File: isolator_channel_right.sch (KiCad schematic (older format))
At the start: 44 parts, among them U301 NE5532, U302 NE5532, U303 NE5532, U304 NE5532, U305 NE5532, U306 NE5532, U307 NE5532, U308 NE5532

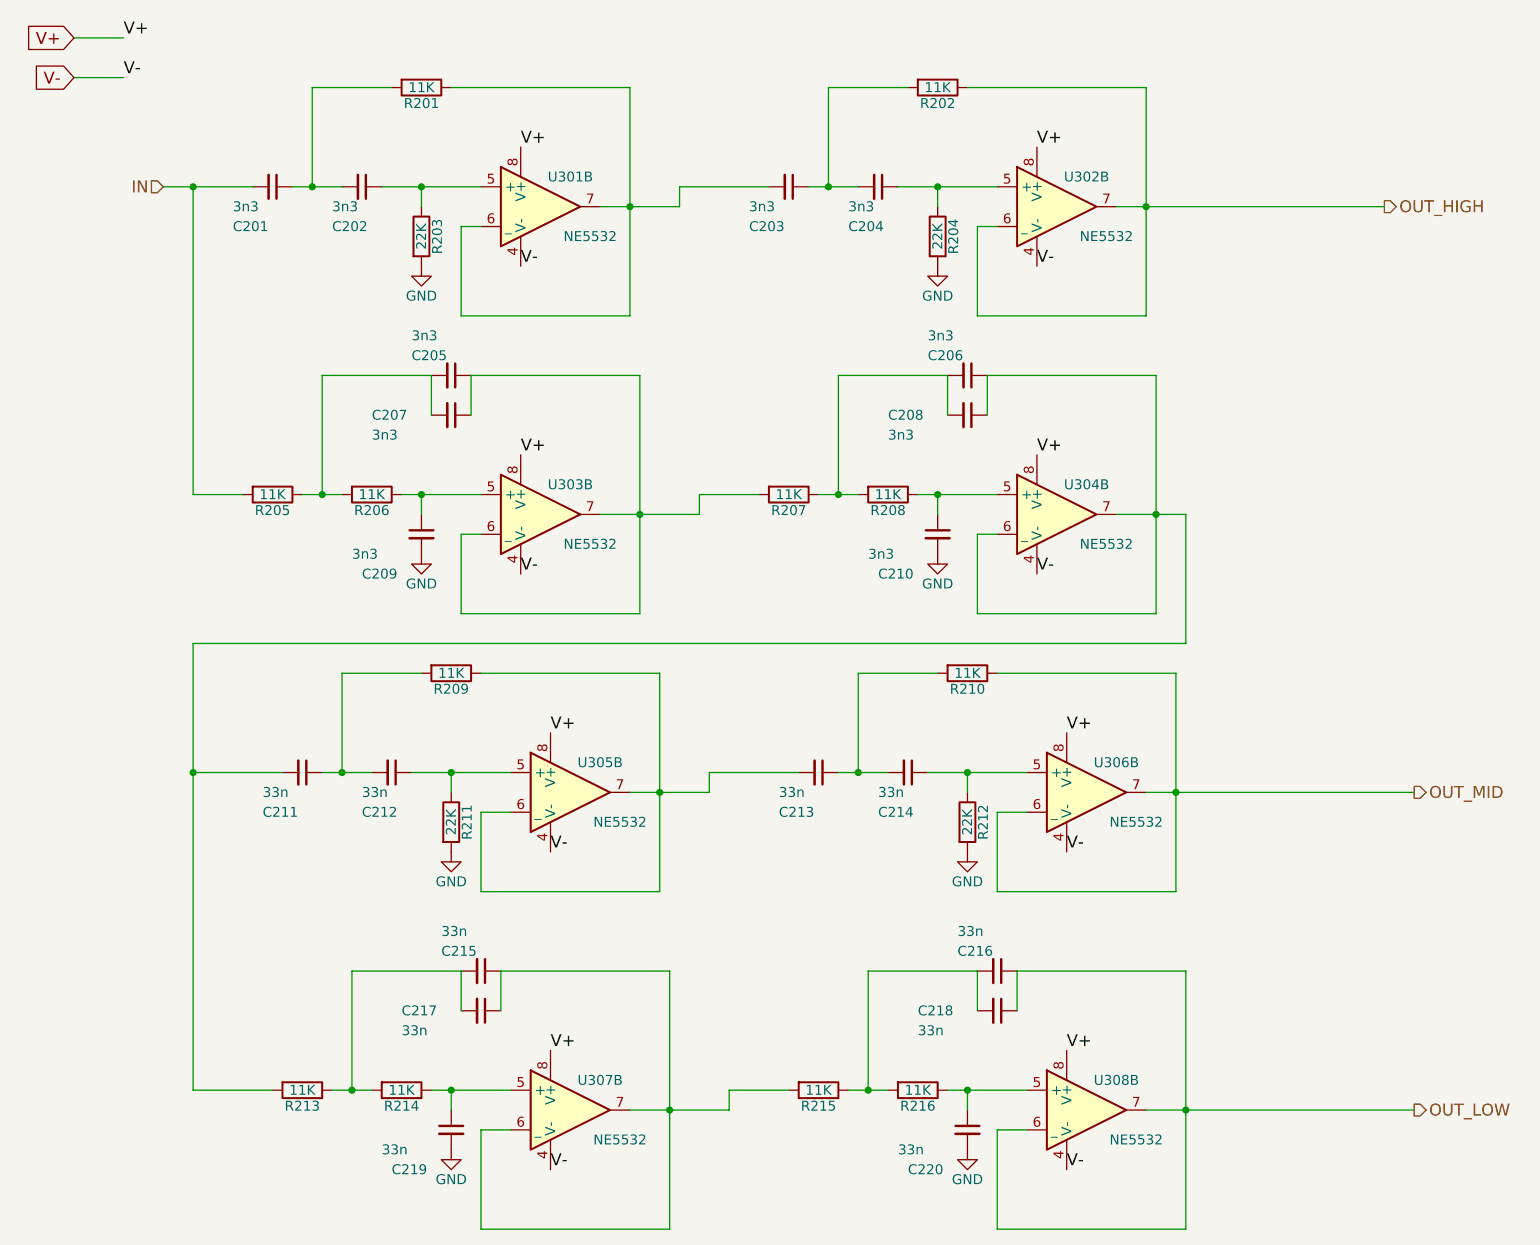
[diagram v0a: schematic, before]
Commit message: Adding active components references
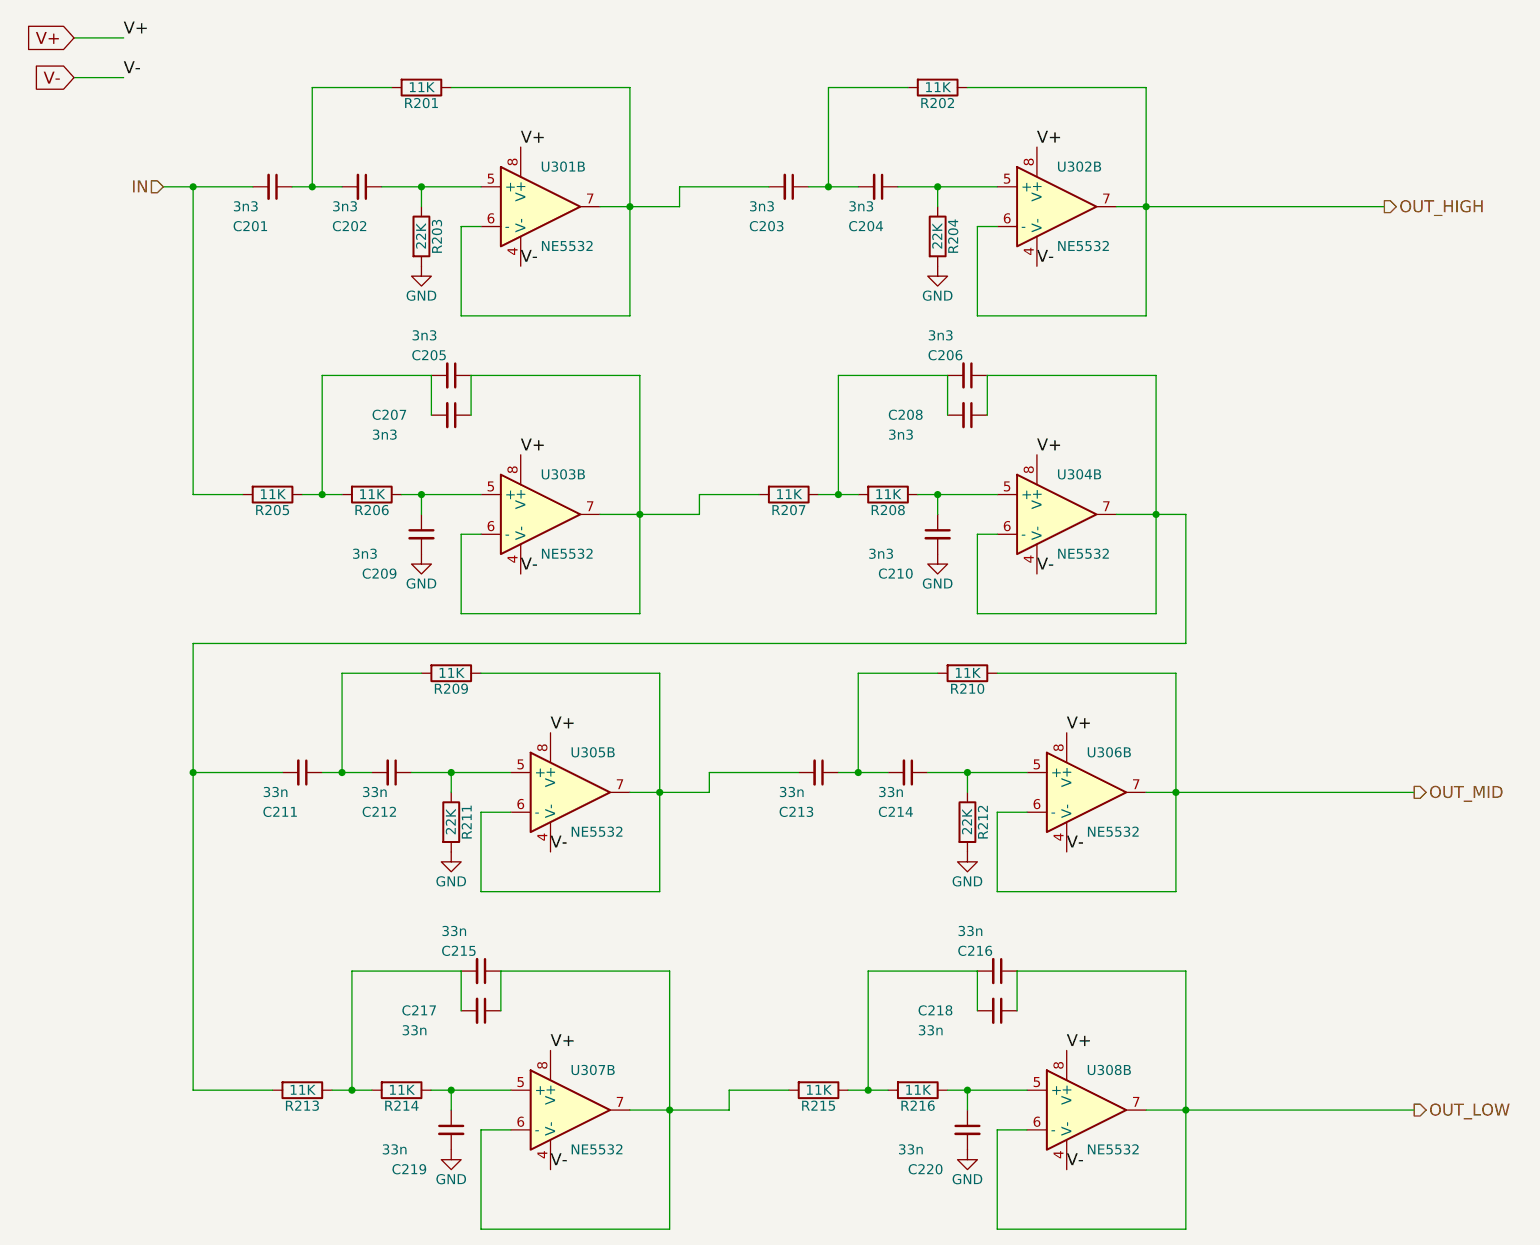
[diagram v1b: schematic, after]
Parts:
- removed U301, U302, U303, U304, U305, U306, U307, U308: NE5532, Housings_DIP:DIP-8_W7.62mm_LongPads, symbol NE5532-RESCUE-isolator
- added U301, U302, U303, U304, U305, U306, U307, U308: NE5532, Housings_DIP:DIP-8_W7.62mm_LongPads, symbol NE5532
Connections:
- net OUT_HIGH: now also U302.6 (-), U302.7
- net OUT_LOW: now also U308.6 (-), U308.7
- net OUT_MID: now also U306.6 (-), U306.7
- net V+: now also U301.8 (V+), U302.8 (V+), U303.8 (V+), U304.8 (V+), U305.8 (V+), U306.8 (V+), U307.8 (V+), U308.8 (V+)
- net V-: now also U301.4 (V-), U302.4 (V-), U303.4 (V-), U304.4 (V-), U305.4 (V-), U306.4 (V-), U307.4 (V-), U308.4 (V-)
- net at C202.1, R203.1: now also U301.5 (+)
- net at C203.2, R201.1: now also U301.6 (-), U301.7
- net at C205.1, C207.1, R207.2: now also U303.6 (-), U303.7
- net at C206.1, C208.1, C211.2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: now also U304.6 (-), U304.7
- net at C212.1, R211.1: now also U305.5 (+)
- net at C213.2, R209.1: now also U305.6 (-), U305.7
- net at C219.1, R214.1: now also U307.5 (+)
- net at C220.1, R216.1: now also U308.5 (+)
- net at C204.1, R204.1: now also U302.5 (+)
- net at C209.1, R206.1: now also U303.5 (+)
- net at C210.1, R208.1: now also U304.5 (+)
- net at C214.1, R212.1: now also U306.5 (+)
- net at C215.1, C217.1, R215.2: now also U307.6 (-), U307.7
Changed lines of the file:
@@
 Text HLabel 7650 6150 2    60   Output ~ 0
 OUT_LOW
-$Comp
-L NE5532-RESCUE-isolator U301
-U 2 1 56D773DB
-P 3250 1600
-AR Path="/56D7589A/56D773DB" Ref="U301"  Part="2"
-AR Path="/56D7630B/56D773DB" Ref="U301"  Part="1"
-AR Path="/56D773DB" Ref="U301"  Part="2"
-F 0 "U301" H 3400 1750 50  0000 C CNN
-F 1 "NE5532" H 3500 1450 50  0000 C CNN
-F 2 "Housings_DIP:DIP-8_W7.62mm_LongPads" H 3250 1600 50  0001 C CNN
-F 3 "" H 3250 1600 50  0000 C CNN
-F 4 "NE5532P" H 3250 1600 60  0001 C CNN "Mfg_Part_No"
-	2    3250 1600
-	1    0    0    -1
-$EndComp
-$Comp
-L NE5532-RESCUE-isolator U302
-U 2 1 56D775D7
-P 5850 1600
-AR Path="/56D7589A/56D775D7" Ref="U302"  Part="2"
-AR Path="/56D7630B/56D775D7" Ref="U302"  Part="1"
-AR Path="/56D775D7" Ref="U302"  Part="2"
-F 0 "U302" H 6000 1750 50  0000 C CNN
-F 1 "NE5532" H 6100 1450 50  0000 C CNN
-F 2 "Housings_DIP:DIP-8_W7.62mm_LongPads" H 5850 1600 50  0001 C CNN
-F 3 "" H 5850 1600 50  0000 C CNN
-F 4 "NE5532P" H 5850 1600 60  0001 C CNN "Mfg_Part_No"
-	2    5850 1600
-	1    0    0    -1
-$EndComp
-$Comp
-L NE5532-RESCUE-isolator U303
-U 2 1 56D776FA
-P 3250 3150
-AR Path="/56D7589A/56D776FA" Ref="U303"  Part="2"
-AR Path="/56D7630B/56D776FA" Ref="U303"  Part="1"
-AR Path="/56D776FA" Ref="U303"  Part="2"
-F 0 "U303" H 3400 3300 50  0000 C CNN
-F 1 "NE5532" H 3500 3000 50  0000 C CNN
-F 2 "Housings_DIP:DIP-8_W7.62mm_LongPads" H 3250 3150 50  0001 C CNN
-F 3 "" H 3250 3150 50  0000 C CNN
-F 4 "NE5532P" H 3250 3150 60  0001 C CNN "Mfg_Part_No"
-	2    3250 3150
-	1    0    0    -1
-$EndComp
-$Comp
-L NE5532-RESCUE-isolator U304
-U 2 1 5707D571
-P 5850 3150
-AR Path="/56D7589A/5707D571" Ref="U304"  Part="2"
-AR Path="/56D7630B/5707D571" Ref="U304"  Part="1"
-AR Path="/5707D571" Ref="U304"  Part="2"
-F 0 "U304" H 6000 3300 50  0000 C CNN
-F 1 "NE5532" H 6100 3000 50  0000 C CNN
-F 2 "Housings_DIP:DIP-8_W7.62mm_LongPads" H 5850 3150 50  0001 C CNN
-F 3 "" H 5850 3150 50  0000 C CNN
-F 4 "NE5532P" H 5850 3150 60  0001 C CNN "Mfg_Part_No"
-	2    5850 3150
-	1    0    0    -1
-$EndComp
-$Comp
-L NE5532-RESCUE-isolator U306
-U 2 1 5707D572
-P 6000 4550
-AR Path="/56D7589A/5707D572" Ref="U306"  Part="2"
-AR Path="/56D7630B/5707D572" Ref="U306"  Part="1"
-AR Path="/5707D572" Ref="U306"  Part="2"
-F 0 "U306" H 6150 4700 50  0000 C CNN
-F 1 "NE5532" H 6250 4400 50  0000 C CNN
-F 2 "Housings_DIP:DIP-8_W7.62mm_LongPads" H 6000 4550 50  0001 C CNN
-F 3 "" H 6000 4550 50  0000 C CNN
-F 4 "NE5532P" H 6000 4550 60  0001 C CNN "Mfg_Part_No"
-	2    6000 4550
-	1    0    0    -1
-$EndComp
-$Comp
-L NE5532-RESCUE-isolator U305
-U 2 1 5707D573
-P 3400 4550
-AR Path="/56D7589A/5707D573" Ref="U305"  Part="2"
-AR Path="/56D7630B/5707D573" Ref="U305"  Part="1"
-AR Path="/5707D573" Ref="U305"  Part="2"
-F 0 "U305" H 3550 4700 50  0000 C CNN
-F 1 "NE5532" H 3650 4400 50  0000 C CNN
-F 2 "Housings_DIP:DIP-8_W7.62mm_LongPads" H 3400 4550 50  0001 C CNN
-F 3 "" H 3400 4550 50  0000 C CNN
-F 4 "NE5532P" H 3400 4550 60  0001 C CNN "Mfg_Part_No"
-	2    3400 4550
-	1    0    0    -1
-$EndComp
-$Comp
-L NE5532-RESCUE-isolator U307
-U 2 1 5707D574
-P 3400 6150
-AR Path="/56D7589A/5707D574" Ref="U307"  Part="2"
-AR Path="/56D7630B/5707D574" Ref="U307"  Part="1"
-AR Path="/5707D574" Ref="U307"  Part="2"
-F 0 "U307" H 3550 6300 50  0000 C CNN
-F 1 "NE5532" H 3650 6000 50  0000 C CNN
-F 2 "Housings_DIP:DIP-8_W7.62mm_LongPads" H 3400 6150 50  0001 C CNN
-F 3 "" H 3400 6150 50  0000 C CNN
-F 4 "NE5532P" H 3400 6150 60  0001 C CNN "Mfg_Part_No"
-	2    3400 6150
-	1    0    0    -1
-$EndComp
-$Comp
-L NE5532-RESCUE-isolator U308
-U 2 1 56D77B5B
-P 6000 6150
-AR Path="/56D7589A/56D77B5B" Ref="U308"  Part="2"
-AR Path="/56D7630B/56D77B5B" Ref="U308"  Part="1"
-AR Path="/56D77B5B" Ref="U308"  Part="2"
-F 0 "U308" H 6150 6300 50  0000 C CNN
-F 1 "NE5532" H 6250 6000 50  0000 C CNN
-F 2 "Housings_DIP:DIP-8_W7.62mm_LongPads" H 6000 6150 50  0001 C CNN
-F 3 "" H 6000 6150 50  0000 C CNN
-F 4 "NE5532P" H 6000 6150 60  0001 C CNN "Mfg_Part_No"
-	2    6000 6150
-	1    0    0    -1
-$EndComp
 Text Label 3150 1300 0    60   ~ 0
 V+
@@
 Wire Wire Line
 	1150 750  900  750
+$Comp
+L NE5532 U301
+U 2 1 5A0D8400
+P 3250 1600
+F 0 "U301" H 3250 1800 50  0000 L CNN
+F 1 "NE5532" H 3250 1400 50  0000 L CNN
+F 2 "Housings_DIP:DIP-8_W7.62mm_LongPads" H 3250 1600 50  0001 C CNN
+F 3 "http://www.ti.com/lit/gpn/ne5532" H 3250 1600 50  0001 C CNN
+F 4 "NE5532P" H 3250 1600 60  0001 C CNN "Mfg_Part_#"
+F 5 "Mouser" H 3250 1600 60  0001 C CNN "Distributor"
+F 6 "595-NE5532P" H 3250 1600 60  0001 C CNN "Distributor Part #"
+F 7 "8-PDIP" H 3250 1600 60  0001 C CNN "Package"
+F 8 "Amplificateurs opérationnels - Amplis-Op Dual Low Noise" H 3250 1600 60  0001 C CNN "Description"
+F 9 "Texas Instruments" H 3250 1600 60  0001 C CNN "Manufacturer"
+	2    3250 1600
+	1    0    0    -1
+$EndComp
+$Comp
+L NE5532 U302
+U 2 1 5A0D8943
+P 5850 1600
+F 0 "U302" H 5850 1800 50  0000 L CNN
+F 1 "NE5532" H 5850 1400 50  0000 L CNN
+F 2 "Housings_DIP:DIP-8_W7.62mm_LongPads" H 5850 1600 50  0001 C CNN
+F 3 "http://www.ti.com/lit/gpn/ne5532" H 5850 1600 50  0001 C CNN
+F 4 "NE5532P" H 5850 1600 60  0001 C CNN "Mfg_Part_#"
+F 5 "Mouser" H 5850 1600 60  0001 C CNN "Distributor"
+F 6 "595-NE5532P" H 5850 1600 60  0001 C CNN "Distributor Part #"
+F 7 "8-PDIP" H 5850 1600 60  0001 C CNN "Package"
+F 8 "Amplificateurs opérationnels - Amplis-Op Dual Low Noise" H 5850 1600 60  0001 C CNN "Description"
+F 9 "Texas Instruments" H 5850 1600 60  0001 C CNN "Manufacturer"
+	2    5850 1600
+	1    0    0    -1
+$EndComp
+$Comp
+L NE5532 U303
+U 2 1 5A0D8BBF
+P 3250 3150
+F 0 "U303" H 3250 3350 50  0000 L CNN
+F 1 "NE5532" H 3250 2950 50  0000 L CNN
+F 2 "Housings_DIP:DIP-8_W7.62mm_LongPads" H 3250 3150 50  0001 C CNN
+F 3 "http://www.ti.com/lit/gpn/ne5532" H 3250 3150 50  0001 C CNN
+F 4 "NE5532P" H 3250 3150 60  0001 C CNN "Mfg_Part_#"
+F 5 "Mouser" H 3250 3150 60  0001 C CNN "Distributor"
+F 6 "595-NE5532P" H 3250 3150 60  0001 C CNN "Distributor Part #"
+F 7 "8-PDIP" H 3250 3150 60  0001 C CNN "Package"
+F 8 "Amplificateurs opérationnels - Amplis-Op Dual Low Noise" H 3250 3150 60  0001 C CNN "Description"
+F 9 "Texas Instruments" H 3250 3150 60  0001 C CNN "Manufacturer"
+	2    3250 3150
+	1    0    0    -1
+$EndComp
+$Comp
+L NE5532 U304
+U 2 1 5A0D8CFE
+P 5850 3150
+F 0 "U304" H 5850 3350 50  0000 L CNN
+F 1 "NE5532" H 5850 2950 50  0000 L CNN
+F 2 "Housings_DIP:DIP-8_W7.62mm_LongPads" H 5850 3150 50  0001 C CNN
+F 3 "http://www.ti.com/lit/gpn/ne5532" H 5850 3150 50  0001 C CNN
+F 4 "NE5532P" H 5850 3150 60  0001 C CNN "Mfg_Part_#"
+F 5 "Mouser" H 5850 3150 60  0001 C CNN "Distributor"
+F 6 "595-NE5532P" H 5850 3150 60  0001 C CNN "Distributor Part #"
+F 7 "8-PDIP" H 5850 3150 60  0001 C CNN "Package"
+F 8 "Amplificateurs opérationnels - Amplis-Op Dual Low Noise" H 5850 3150 60  0001 C CNN "Description"
+F 9 "Texas Instruments" H 5850 3150 60  0001 C CNN "Manufacturer"
+	2    5850 3150
+	1    0    0    -1
+$EndComp
+$Comp
+L NE5532 U305
+U 2 1 5A0D915D
+P 3400 4550
+F 0 "U305" H 3400 4750 50  0000 L CNN
+F 1 "NE5532" H 3400 4350 50  0000 L CNN
+F 2 "Housings_DIP:DIP-8_W7.62mm_LongPads" H 3400 4550 50  0001 C CNN
+F 3 "http://www.ti.com/lit/gpn/ne5532" H 3400 4550 50  0001 C CNN
+F 4 "NE5532P" H 3400 4550 60  0001 C CNN "Mfg_Part_#"
+F 5 "Mouser" H 3400 4550 60  0001 C CNN "Distributor"
+F 6 "595-NE5532P" H 3400 4550 60  0001 C CNN "Distributor Part #"
+F 7 "8-PDIP" H 3400 4550 60  0001 C CNN "Package"
+F 8 "Amplificateurs opérationnels - Amplis-Op Dual Low Noise" H 3400 4550 60  0001 C CNN "Description"
+F 9 "Texas Instruments" H 3400 4550 60  0001 C CNN "Manufacturer"
+	2    3400 4550
+	1    0    0    -1
+$EndComp
+$Comp
+L NE5532 U306
+U 2 1 5A0D91FE
+P 6000 4550
+F 0 "U306" H 6000 4750 50  0000 L CNN
+F 1 "NE5532" H 6000 4350 50  0000 L CNN
+F 2 "Housings_DIP:DIP-8_W7.62mm_LongPads" H 6000 4550 50  0001 C CNN
+F 3 "http://www.ti.com/lit/gpn/ne5532" H 6000 4550 50  0001 C CNN
+F 4 "NE5532P" H 6000 4550 60  0001 C CNN "Mfg_Part_#"
+F 5 "Mouser" H 6000 4550 60  0001 C CNN "Distributor"
+F 6 "595-NE5532P" H 6000 4550 60  0001 C CNN "Distributor Part #"
+F 7 "8-PDIP" H 6000 4550 60  0001 C CNN "Package"
+F 8 "Amplificateurs opérationnels - Amplis-Op Dual Low Noise" H 6000 4550 60  0001 C CNN "Description"
+F 9 "Texas Instruments" H 6000 4550 60  0001 C CNN "Manufacturer"
+	2    6000 4550
+	1    0    0    -1
+$EndComp
+$Comp
+L NE5532 U307
+U 2 1 5A0D9605
+P 3400 6150
+F 0 "U307" H 3400 6350 50  0000 L CNN
+F 1 "NE5532" H 3400 5950 50  0000 L CNN
+F 2 "Housings_DIP:DIP-8_W7.62mm_LongPads" H 3400 6150 50  0001 C CNN
+F 3 "http://www.ti.com/lit/gpn/ne5532" H 3400 6150 50  0001 C CNN
+F 4 "NE5532P" H 3400 6150 60  0001 C CNN "Mfg_Part_#"
+F 5 "Mouser" H 3400 6150 60  0001 C CNN "Distributor"
+F 6 "595-NE5532P" H 3400 6150 60  0001 C CNN "Distributor Part #"
+F 7 "8-PDIP" H 3400 6150 60  0001 C CNN "Package"
+F 8 "Amplificateurs opérationnels - Amplis-Op Dual Low Noise" H 3400 6150 60  0001 C CNN "Description"
+F 9 "Texas Instruments" H 3400 6150 60  0001 C CNN "Manufacturer"
+	2    3400 6150
+	1    0    0    -1
+$EndComp
+$Comp
+L NE5532 U308
+U 2 1 5A0D96AC
+P 6000 6150
+F 0 "U308" H 6000 6350 50  0000 L CNN
+F 1 "NE5532" H 6000 5950 50  0000 L CNN
+F 2 "Housings_DIP:DIP-8_W7.62mm_LongPads" H 6000 6150 50  0001 C CNN
+F 3 "http://www.ti.com/lit/gpn/ne5532" H 6000 6150 50  0001 C CNN
+F 4 "NE5532P" H 6000 6150 60  0001 C CNN "Mfg_Part_#"
+F 5 "Mouser" H 6000 6150 60  0001 C CNN "Distributor"
+F 6 "595-NE5532P" H 6000 6150 60  0001 C CNN "Distributor Part #"
+F 7 "8-PDIP" H 6000 6150 60  0001 C CNN "Package"
+F 8 "Amplificateurs opérationnels - Amplis-Op Dual Low Noise" H 6000 6150 60  0001 C CNN "Description"
+F 9 "Texas Instruments" H 6000 6150 60  0001 C CNN "Manufacturer"
+	2    6000 6150
+	1    0    0    -1
+$EndComp
 $EndSCHEMATC

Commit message: Updating components references and properties
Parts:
- C201, C202, C203, C204, C205, C206, C207, C208, C209, C210, C211, C212, C213, C214, C215, C216, C217, C218, C219, C220: footprint Capacitors_ThroughHole:C_Rect_L7_W3.5_P5 -> Capacitors_THT:C_Rect_L7.0mm_W3.5mm_P5.00mm
- R201, R202, R203, R204, R205, R206, R207, R208, R209, R210, R211, R212, R213, R214, R215, R216: footprint Resistors_ThroughHole:Resistor_Horizontal_RM7mm -> Resistors_THT:R_Axial_DIN0204_L3.6mm_D1.6mm_P5.08mm_Horizontal
